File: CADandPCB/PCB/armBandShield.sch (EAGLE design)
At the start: 20 parts

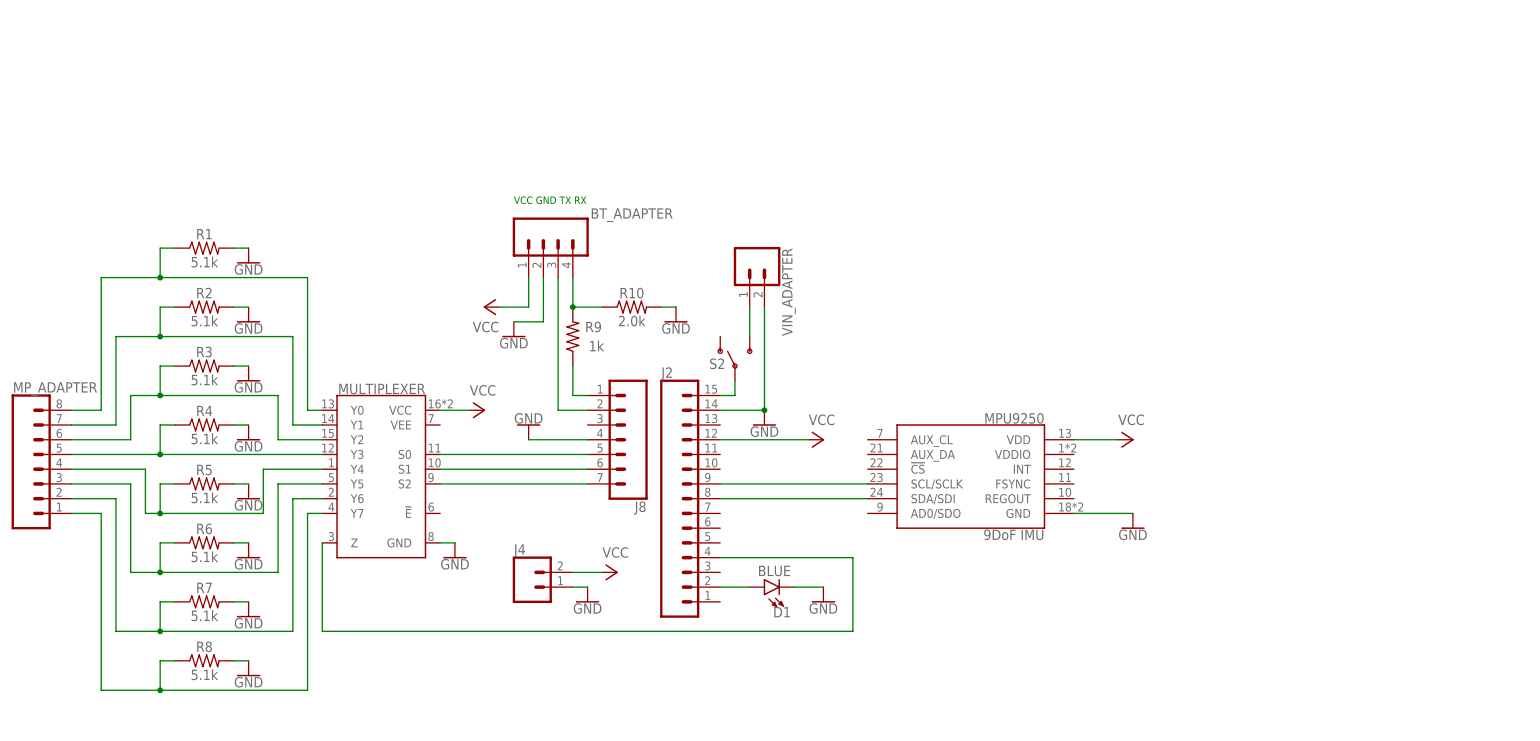
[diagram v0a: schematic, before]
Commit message: Clean up schematic using labels. Remove old board. Prepare for breakout.
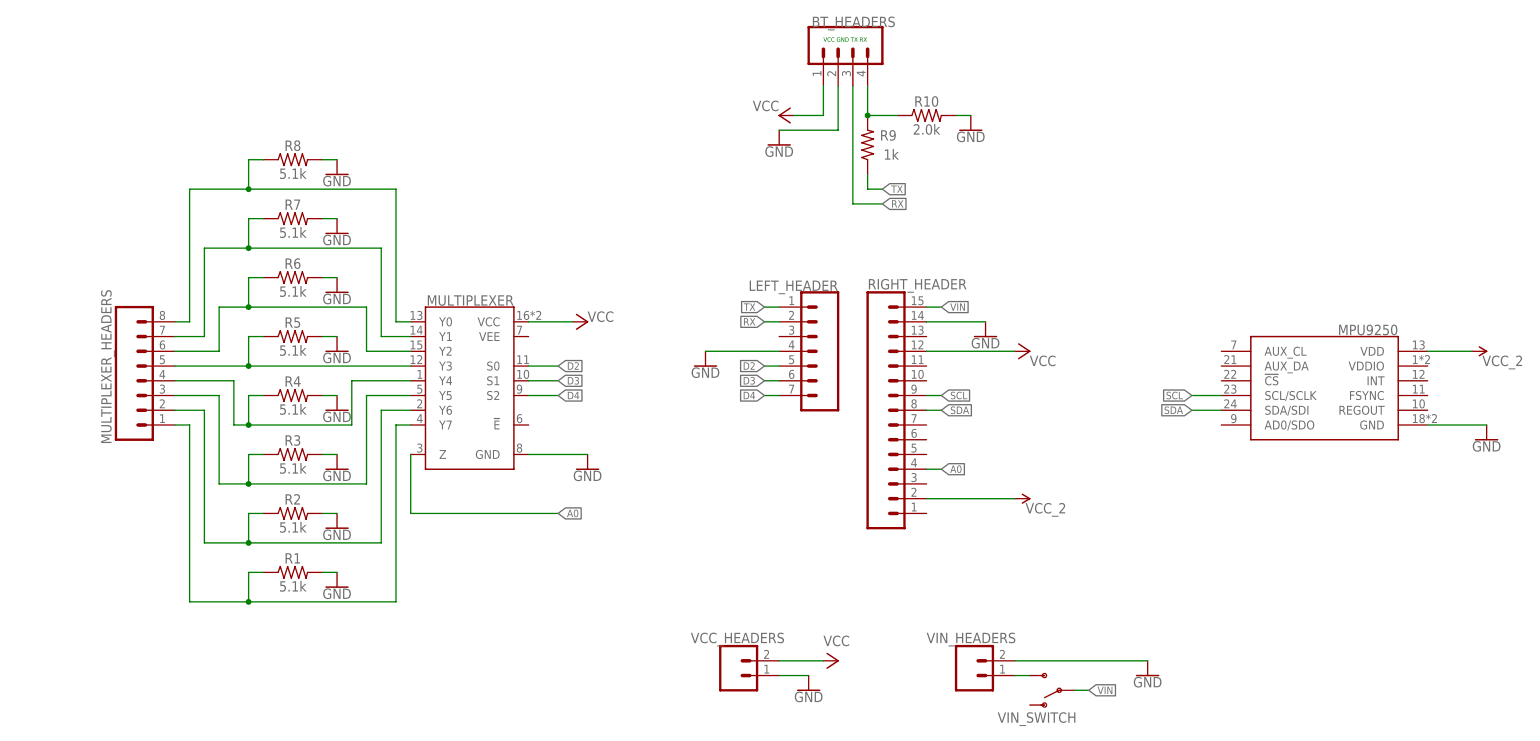
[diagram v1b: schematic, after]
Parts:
- removed BT_ADAPTER: (no value), SparkFun-Connectors:CONN_04
- removed D1: BLUE, SparkFun-LED:LED-BLUE1206
- removed J2: (no value), SparkFun-Connectors:CONN_15
- removed J4: (no value), SparkFun-Connectors:CONN_02
- removed J8: (no value), SparkFun-Connectors:CONN_07
- removed MP_ADAPTER: (no value), SparkFun-Connectors:CONN_08"
- removed S2: (no value), SparkFun-Switches:SWITCH-SPDT-SMD-RIGHT-ANGLE
- removed VIN_ADAPTER: (no value), SparkFun-Connectors:CONN_02PTH3
- added BT_HEADERS: (no value), SparkFun-Connectors:CONN_04
- added LEFT_HEADER: (no value), SparkFun-Connectors:CONN_07
- added MULTIPLEXER_HEADERS: (no value), SparkFun-Connectors:CONN_08"
- added RIGHT_HEADER: (no value), SparkFun-Connectors:CONN_15
- added VCC_HEADERS: (no value), SparkFun-Connectors:CONN_02
- added VIN_HEADERS: (no value), SparkFun-Connectors:CONN_02PTH3
- added VIN_SWITCH: (no value), SparkFun-Switches:SWITCH-SPDT-SMD-RIGHT-ANGLE
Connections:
- removed net MP0: J8.5, MULTIPLEXER.S0
- removed net MP1: J8.6, MULTIPLEXER.S1
- removed net MP2: J8.7, MULTIPLEXER.S2
- removed net N$25: J2.15, S2.P
- removed net N$28: J2.4, MULTIPLEXER.Z
- removed net N$8: D1.A, J2.2
- removed net RX_TX: BT_ADAPTER.3, J8.2
- removed net TX_RX: J8.1, R9.1
- new net A0: MULTIPLEXER.Z, RIGHT_HEADER.4
- new net D2: LEFT_HEADER.5, MULTIPLEXER.S0
- new net D3: LEFT_HEADER.6, MULTIPLEXER.S1
- new net D4: LEFT_HEADER.7, MULTIPLEXER.S2
- new net RX: BT_HEADERS.3, LEFT_HEADER.2
- new net TX: LEFT_HEADER.1, R9.1
- new net VCC_2: MPU9250.VDD, RIGHT_HEADER.2
- new net VIN: RIGHT_HEADER.15, VIN_SWITCH.P
- net FSR1: now also MULTIPLEXER_HEADERS.1, R1.1; no longer MP_ADAPTER.1, R8.1
- net FSR2: now also MULTIPLEXER_HEADERS.2, R2.1; no longer MP_ADAPTER.2, R7.1
- net FSR3: now also MULTIPLEXER_HEADERS.3, R3.1; no longer MP_ADAPTER.3, R6.1
- net FSR4: now also MULTIPLEXER_HEADERS.4, R4.1; no longer MP_ADAPTER.4, R5.1
- net FSR5: now also MULTIPLEXER_HEADERS.5, R5.1; no longer MP_ADAPTER.5, R4.1
- net FSR6: now also MULTIPLEXER_HEADERS.6, R6.1; no longer MP_ADAPTER.6, R3.1
- net FSR7: now also MULTIPLEXER_HEADERS.7, R7.1; no longer MP_ADAPTER.7, R2.1
- net FSR8: now also MULTIPLEXER_HEADERS.8, R8.1; no longer MP_ADAPTER.8, R1.1
- net GND: now also BT_HEADERS.2, LEFT_HEADER.4, RIGHT_HEADER.14, VCC_HEADERS.1, VIN_HEADERS.2; no longer BT_ADAPTER.2, D1.C, J2.14, J4.1, J8.4, VIN_ADAPTER.2
- net N$1: now also VIN_HEADERS.1, VIN_SWITCH.S; no longer S2.S, VIN_ADAPTER.1
- net N$7: now also BT_HEADERS.4; no longer BT_ADAPTER.4
- net SCL: now also RIGHT_HEADER.9; no longer J2.9
- net SDA: now also RIGHT_HEADER.8; no longer J2.8
- net VCC: now also BT_HEADERS.1, RIGHT_HEADER.12, VCC_HEADERS.2; no longer BT_ADAPTER.1, J2.12, J4.2, MPU9250.VDD
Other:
- moved on the sheet: MPU9250, MULTIPLEXER, R1, R10, R2, R3, R4, R5, R6, R7, R8, R9

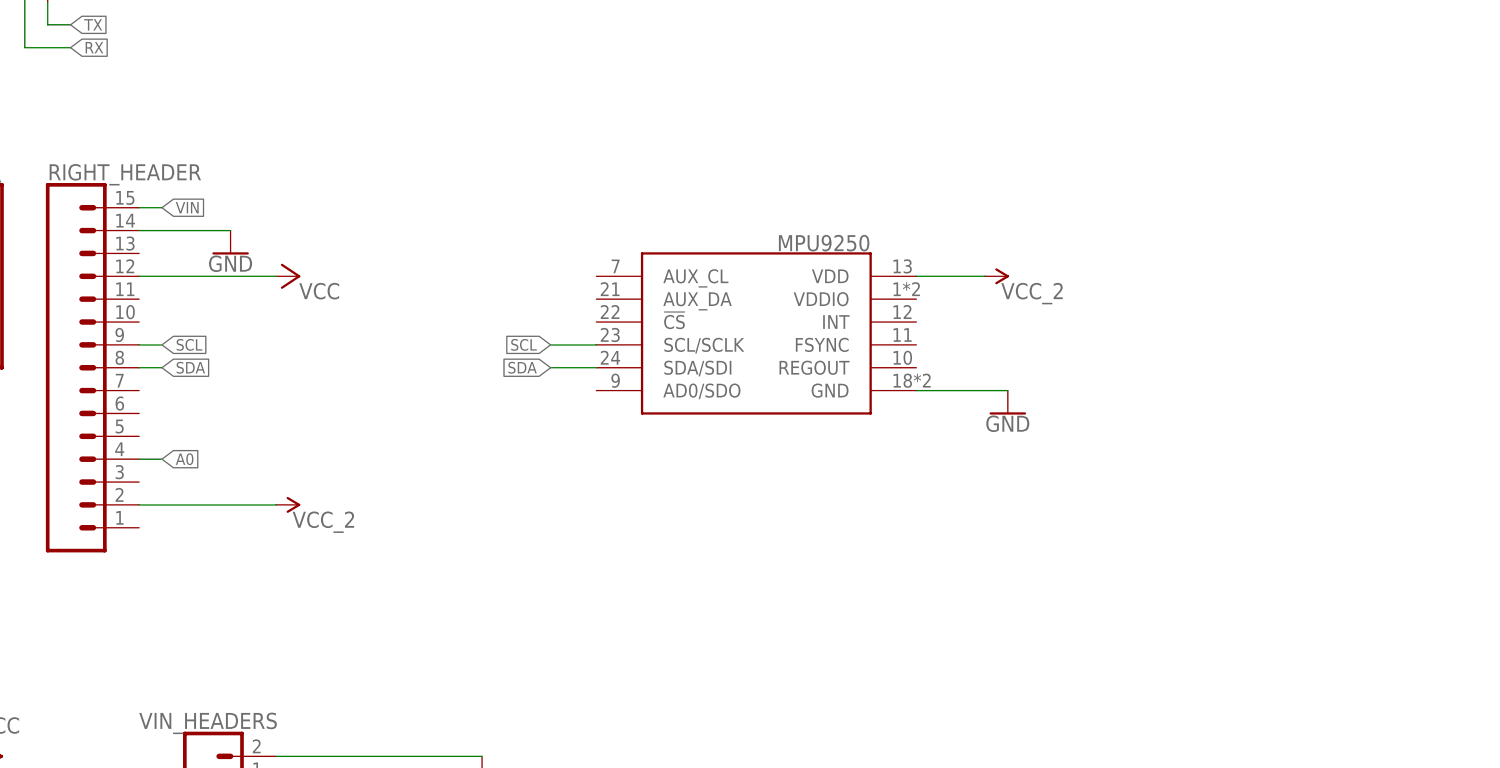
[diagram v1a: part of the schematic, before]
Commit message: Added required breakout components for MPU 9250
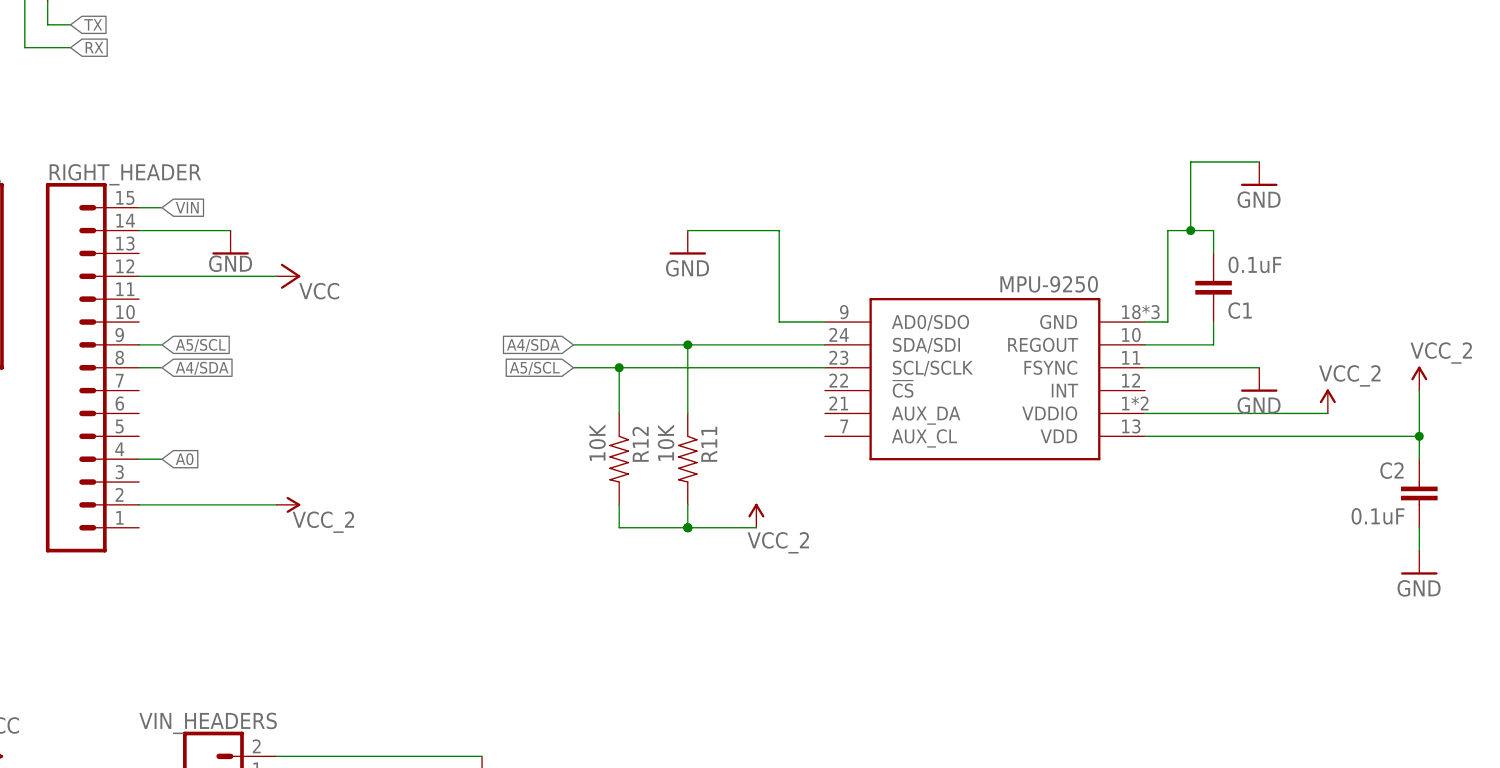
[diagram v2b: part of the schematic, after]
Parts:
- removed MPU9250: 9DoF IMU, SparkFun-Sensors:MPU-9250
- added C1, C2: 0.1uF, SparkFun-Capacitors:0.1UF-25V(+80/-20%)(0603)
- added R11, R12: 10K, SparkFun-Resistors:10KOHM-1/10W-1%(0603)0603
- added U1: MPU-9250, Testing:MPU-9250
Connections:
- removed net SCL: MPU9250.SCL/SCLK, RIGHT_HEADER.9
- removed net SDA: MPU9250.SDA/SDI, RIGHT_HEADER.8
- new net A4/SDA: R11.1, RIGHT_HEADER.8, U1.SDA/SDI
- new net A5/SCL: R12.1, RIGHT_HEADER.9, U1.SCL/SCLK
- new net REGOUT: C1.1, U1.REGOUT
- net GND: now also C1.2, C2.2, U1.AD0/SDO, U1.FSYNC, U1.GND; no longer MPU9250.GND
- net VCC_2: now also C2.1, R11.2, R12.2, U1.VDD, U1.VDDIO; no longer MPU9250.VDD

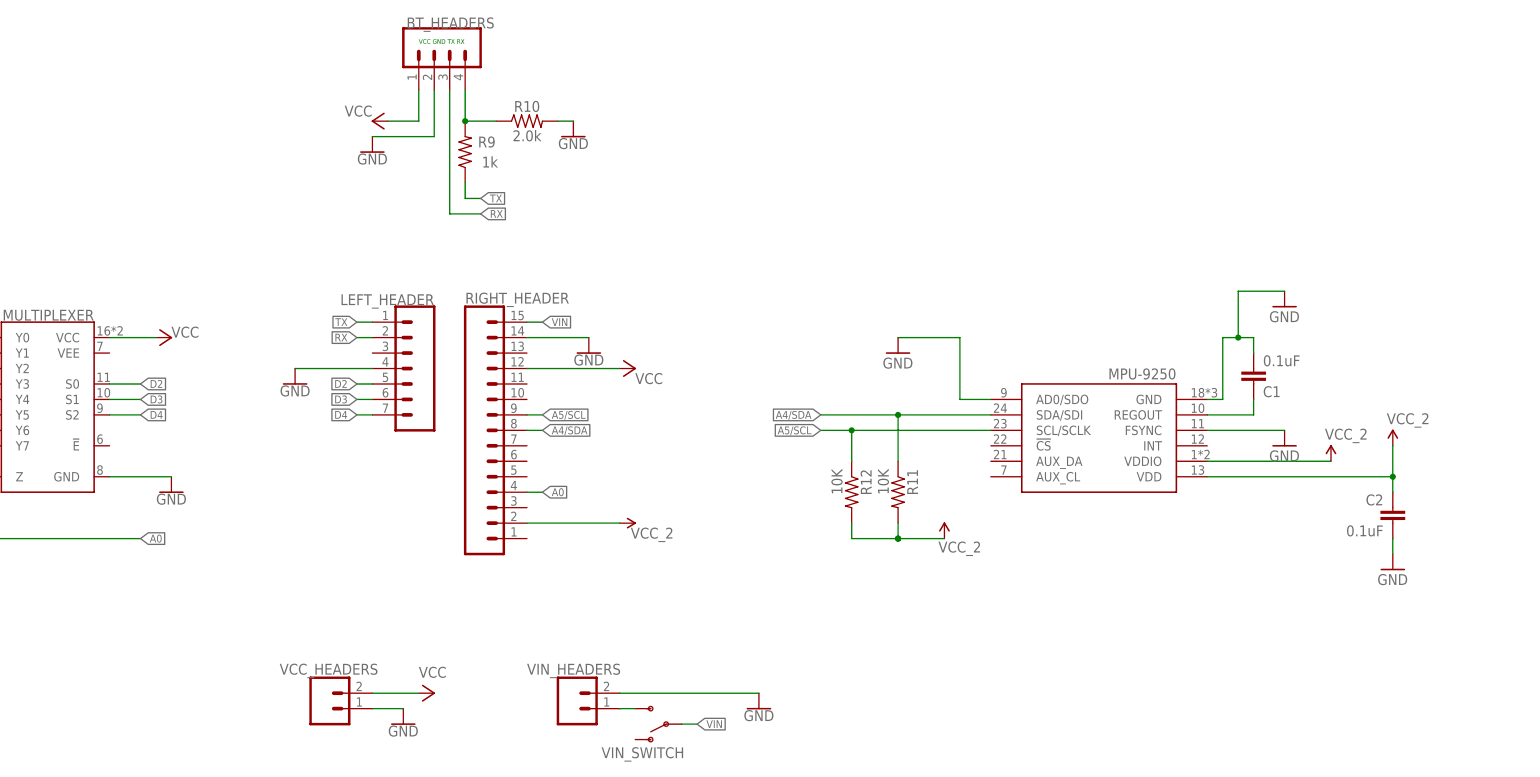
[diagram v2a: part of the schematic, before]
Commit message: Added required breakout components for Multixplexer
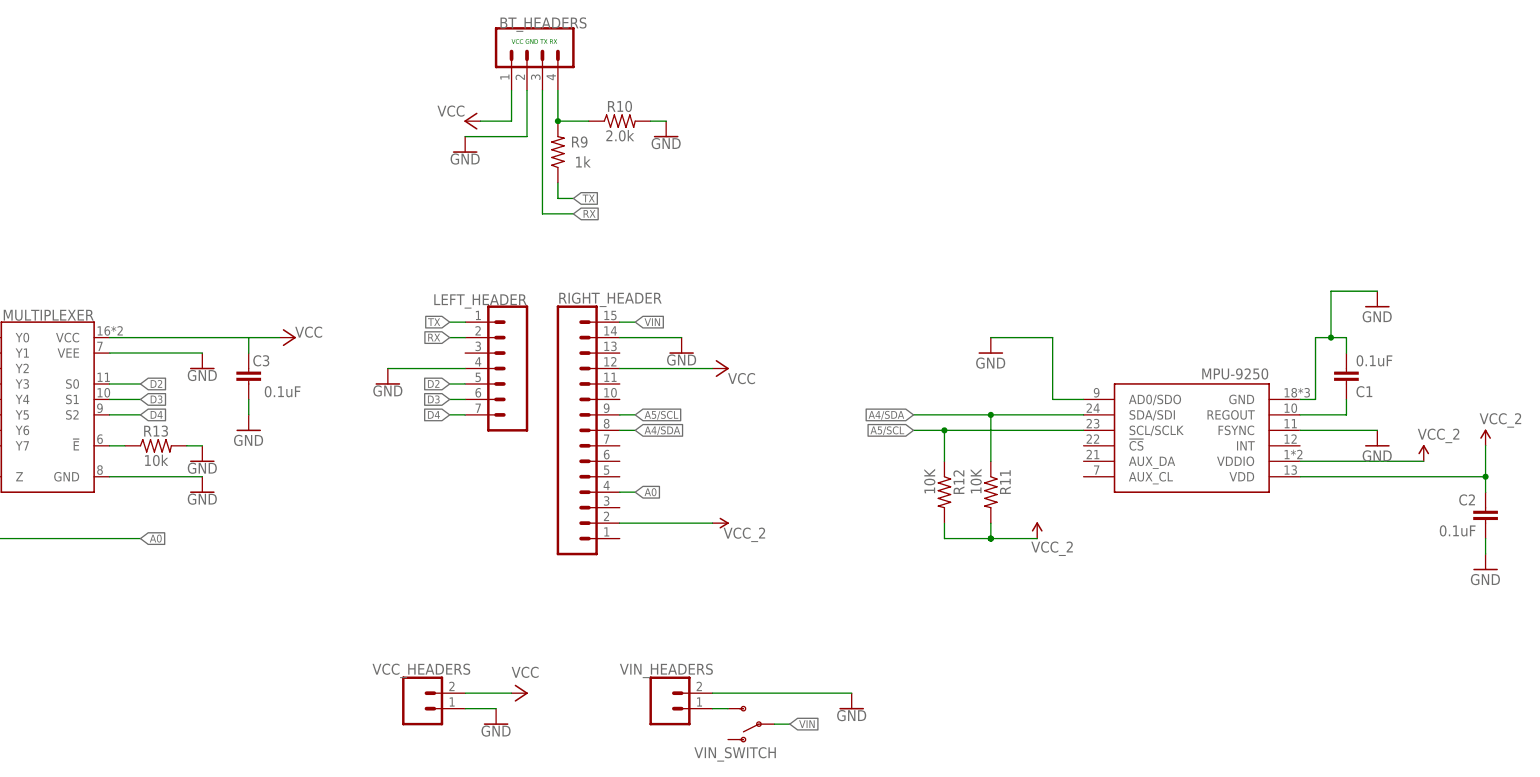
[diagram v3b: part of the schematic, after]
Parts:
- added C3: 0.1uF, SparkFun-Capacitors:0.1UF-25V(+80/-20%)(0603)
- added R13: 10k, SparkFun-Resistors:10KOHM-0603-1/10W-1%
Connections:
- new net N$2: MULTIPLEXER.!E!, R13.1
- new net VCC_1: C3.1
- net GND: now also C3.2, MULTIPLEXER.VEE, R13.2
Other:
- moved on the sheet: BT_HEADERS, C1, C2, LEFT_HEADER, R10, R11, R12, R9, RIGHT_HEADER, VCC_HEADERS, VIN_HEADERS, VIN_SWITCH

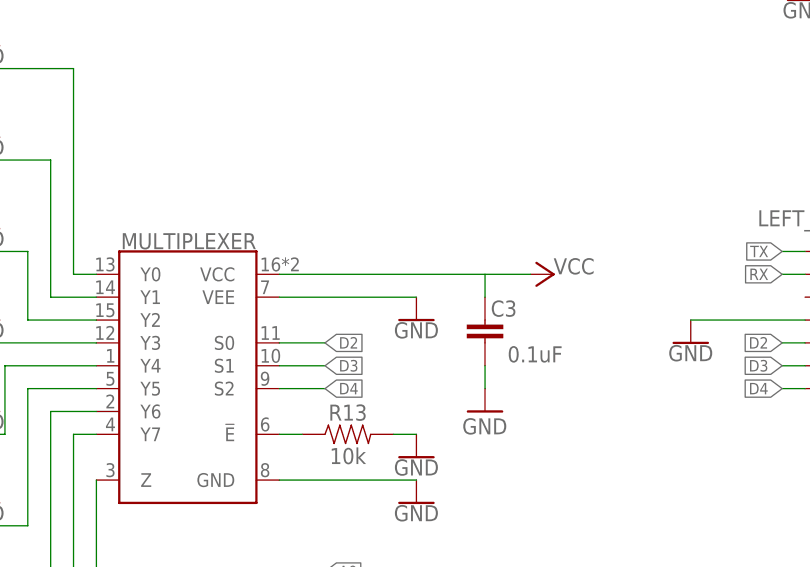
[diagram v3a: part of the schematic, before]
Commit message: Initial board lay out and .brd commit
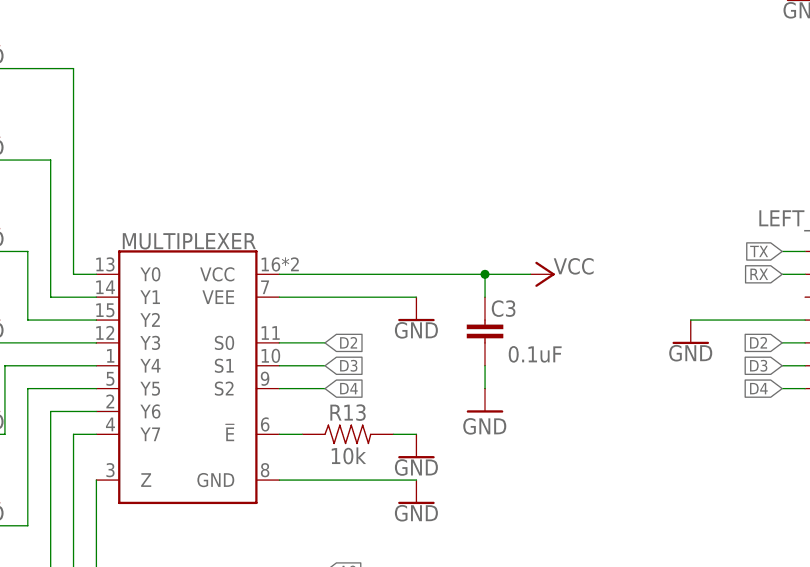
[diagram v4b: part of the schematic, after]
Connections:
- removed net VCC_1: C3.1
- net VCC: now also C3.1
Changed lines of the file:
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@@
 <pinref part="MULTIPLEXER" gate="G$1" pin="VCC"/>
 <pinref part="P+3" gate="VCC" pin="VCC"/>
-<wire x1="73.66" y1="63.5" x2="101.6" y2="63.5" width="0.1524" layer="91"/>
+<wire x1="73.66" y1="63.5" x2="96.52" y2="63.5" width="0.1524" layer="91"/>
+<pinref part="C3" gate="G$1" pin="1"/>
+<wire x1="96.52" y1="63.5" x2="101.6" y2="63.5" width="0.1524" layer="91"/>
+<wire x1="96.52" y1="60.96" x2="96.52" y2="63.5" width="0.1524" layer="91"/>
+<junction x="96.52" y="63.5"/>
 </segment>
 <segment>
@@
 </segment>
 </net>
-<net name="VCC_1" class="0">
-<segment>
-<pinref part="C3" gate="G$1" pin="1"/>
-<wire x1="96.52" y1="63.5" x2="96.52" y2="60.96" width="0.1524" layer="91"/>
-</segment>
-</net>
